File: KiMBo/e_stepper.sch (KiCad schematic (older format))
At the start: 24 parts, among them U19 TMC2130

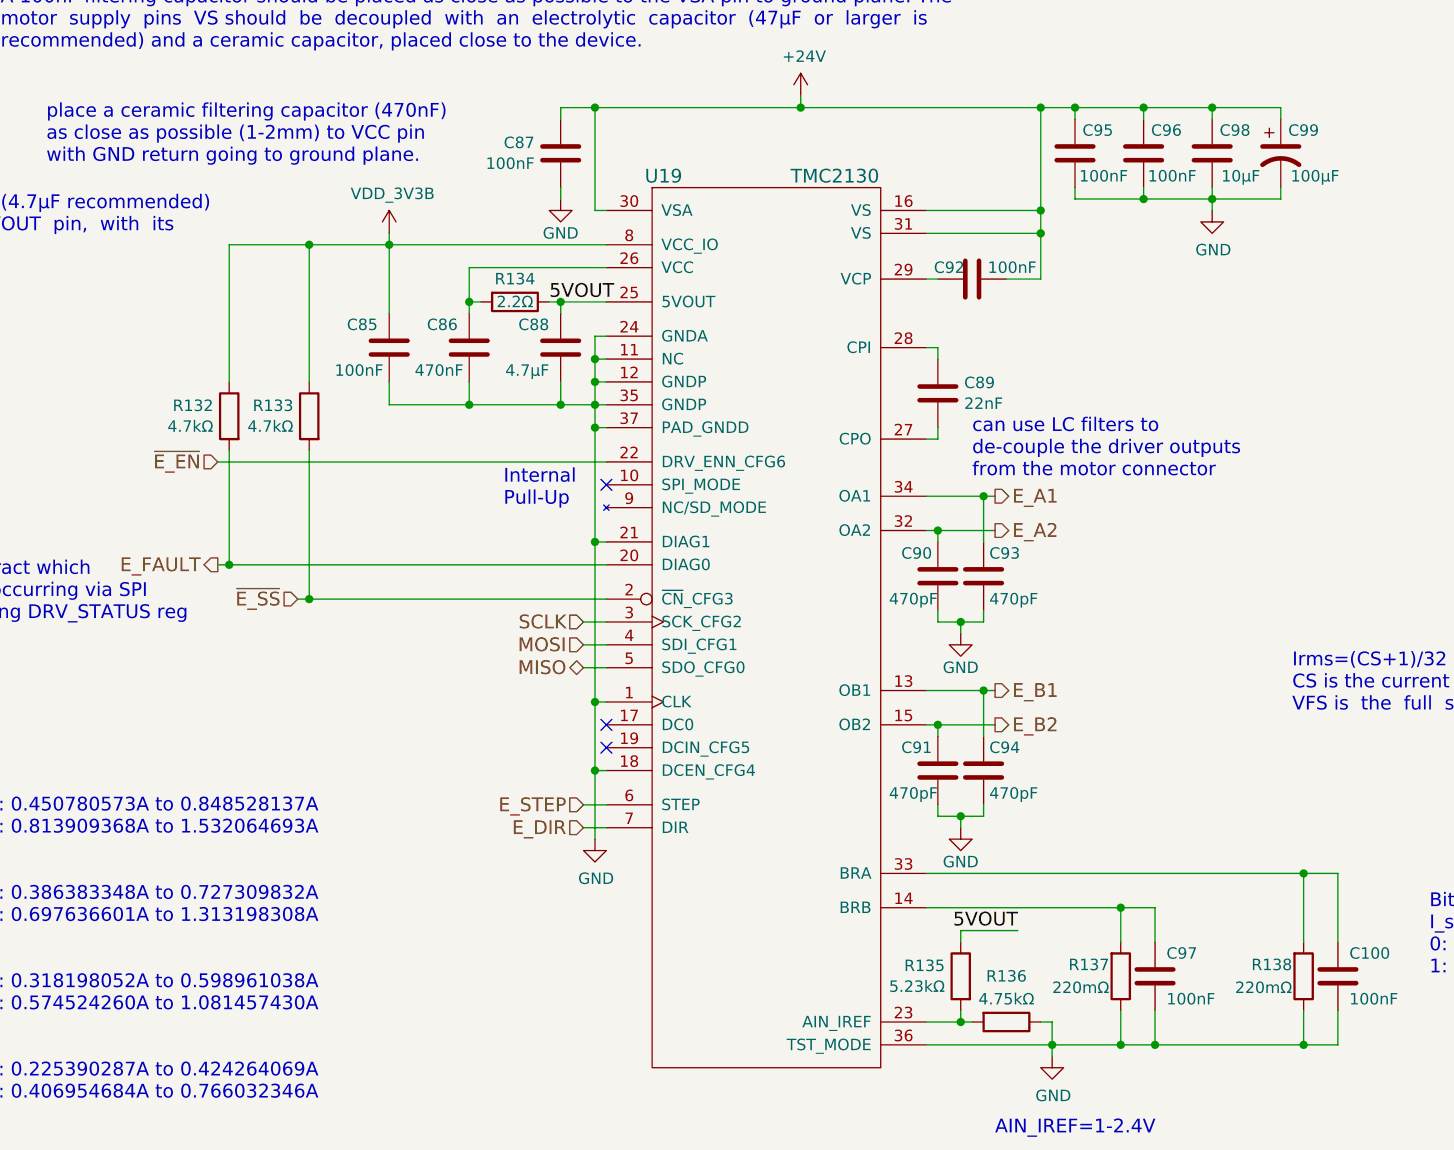
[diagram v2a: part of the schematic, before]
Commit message: Leave SPI0 free for a display, reassign pins so SPI1 is available
Fix some typos/errors
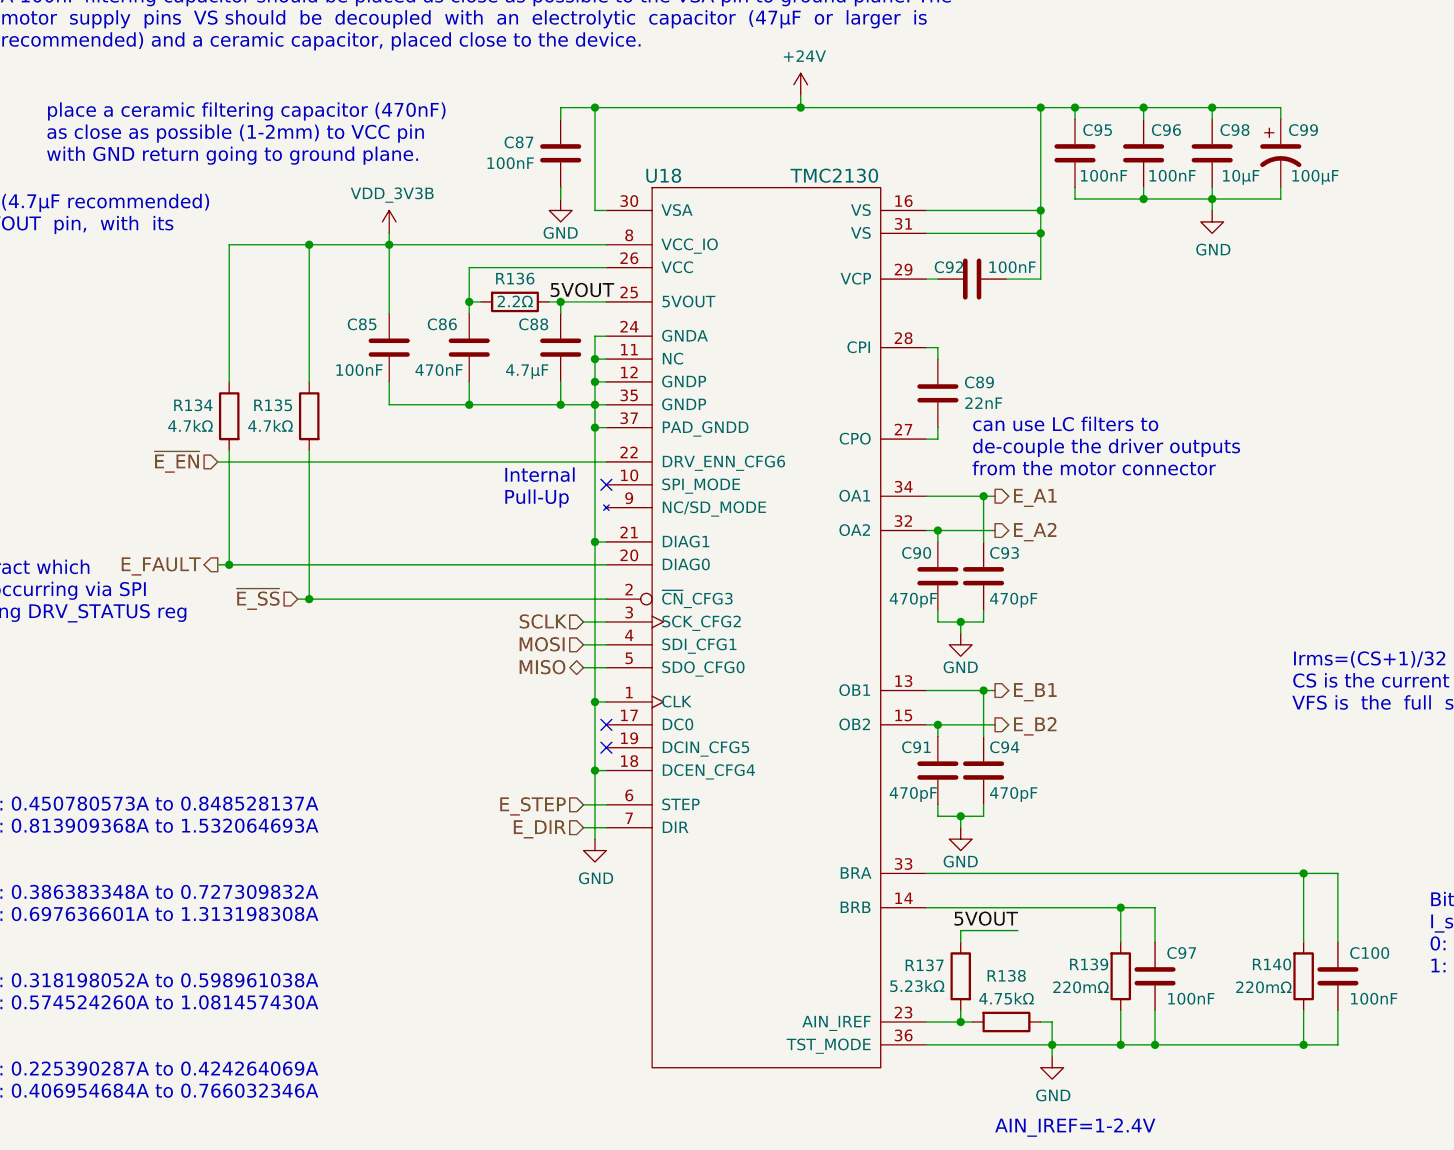
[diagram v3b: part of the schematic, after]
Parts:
- renumbered R132 to R134, R133 to R135, R134 to R136, R135 to R137, R136 to R138, R137 to R139, R138 to R140, U19 to U18
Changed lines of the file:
@@
 $EndComp
 $Comp
-L GND #PWR0200
+L GND #PWR0199
 U 1 1 589BD203
 P 7300 4150
-F 0 "#PWR0200" H 7300 3900 50  0001 C CNN
+F 0 "#PWR0199" H 7300 3900 50  0001 C CNN
 F 1 "GND" H 7300 4000 50  0000 C CNN
 F 2 "" H 7300 4150 50  0000 C CNN
@@
 $EndComp
 $Comp
-L GND #PWR0201
+L GND #PWR0200
 U 1 1 589BE47E
 P 10150 4200
-F 0 "#PWR0201" H 10150 3950 50  0001 C CNN
+F 0 "#PWR0200" H 10150 3950 50  0001 C CNN
 F 1 "GND" H 10155 4027 50  0000 C CNN
 F 2 "" H 10150 4200 50  0000 C CNN
@@
 $EndComp
 $Comp
-L +24V #PWR0202
+L +24V #PWR0201
 U 1 1 5BA7E125
 P 8350 3700
-F 0 "#PWR0202" H 8350 3550 50  0001 C CNN
+F 0 "#PWR0201" H 8350 3550 50  0001 C CNN
 F 1 "+24V" H 8365 3873 50  0000 C CNN
 F 2 "" H 8350 3700 50  0000 C CNN
@@
 $EndComp
 $Comp
-L R R138
+L R R140
 U 1 1 589C1BED
 P 10550 7550
-F 0 "R138" H 10500 7500 50  0000 R CNN
+F 0 "R140" H 10500 7500 50  0000 R CNN
 F 1 "220mΩ" H 10500 7600 50  0000 R CNN
 F 2 "" V 10480 7550 50  0001 C CNN
@@
 $EndComp
 $Comp
-L R R137
+L R R139
 U 1 1 589C1CA7
 P 9750 7550
-F 0 "R137" H 9700 7500 50  0000 R CNN
+F 0 "R139" H 9700 7500 50  0000 R CNN
 F 1 "220mΩ" H 9700 7600 50  0000 R CNN
 F 2 "" V 9680 7550 50  0001 C CNN
@@
 $EndComp
 $Comp
-L GND #PWR0203
+L GND #PWR0202
 U 1 1 5BA7E129
 P 9450 7900
-F 0 "#PWR0203" H 9450 7650 50  0001 C CNN
+F 0 "#PWR0202" H 9450 7650 50  0001 C CNN
 F 1 "GND" H 9455 7727 50  0000 C CNN
 F 2 "" H 9450 7900 50  0000 C CNN
@@
 NoConn ~ 7500 6450
 $Comp
-L R R134
+L R R136
 U 1 1 5BA7E12B
 P 7100 4600
-F 0 "R134" V 7000 4600 50  0000 C CNN
+F 0 "R136" V 7000 4600 50  0000 C CNN
 F 1 "2.2Ω" V 7100 4600 50  0000 C CNN
 F 2 "" V 7030 4600 50  0001 C CNN
@@
 NoConn ~ 7500 6550
 $Comp
-L GND #PWR0204
+L GND #PWR0203
 U 1 1 589C97FF
 P 7450 6950
-F 0 "#PWR0204" H 7450 6700 50  0001 C CNN
+F 0 "#PWR0203" H 7450 6700 50  0001 C CNN
 F 1 "GND" H 7455 6777 50  0000 C CNN
 F 2 "" H 7450 6950 50  0000 C CNN
@@
 E_FAULT
 $Comp
-L R R132
+L R R134
 U 1 1 589D21BC
 P 5850 5100
-F 0 "R132" H 5919 5146 50  0000 L CNN
+F 0 "R134" H 5919 5146 50  0000 L CNN
 F 1 "4.7kΩ" H 5919 5055 50  0000 L CNN
 F 2 "" V 5780 5100 50  0001 C CNN
@@
 5VOUT
 $Comp
-L R R135
+L R R137
 U 1 1 589E13FD
 P 9050 7550
-F 0 "R135" H 9119 7596 50  0000 L CNN
+F 0 "R137" H 9119 7596 50  0000 L CNN
 F 1 "5.23kΩ" H 9119 7505 50  0000 L CNN
 F 2 "" V 8980 7550 50  0001 C CNN
@@
 5VOUT
 $Comp
-L R R136
+L R R138
 U 1 1 589E24D4
 P 9250 7750
-F 0 "R136" V 9050 7750 50  0000 C CNN
+F 0 "R138" V 9050 7750 50  0000 C CNN
 F 1 "4.75kΩ" V 9150 7750 50  0000 C CNN
 F 2 "" V 9180 7750 50  0001 C CNN
@@
 AIN_IREF=1-2.4V
 $Comp
-L R R133
+L R R135
 U 1 1 5BA7E132
 P 6200 5100
-F 0 "R133" H 6269 5146 50  0000 L CNN
+F 0 "R135" H 6269 5146 50  0000 L CNN
 F 1 "4.7kΩ" H 6269 5055 50  0000 L CNN
 F 2 "" V 6130 5100 50  0001 C CNN
@@
 $EndComp
 $Comp
-L GND #PWR0205
+L GND #PWR0204
 U 1 1 58B19D33
 P 9050 6050
-F 0 "#PWR0205" H 9050 5800 50  0001 C CNN
+F 0 "#PWR0204" H 9050 5800 50  0001 C CNN
 F 1 "GND" H 9050 5900 50  0000 C CNN
 F 2 "" H 9050 6050 50  0000 C CNN
@@
 $EndComp
 $Comp
-L GND #PWR0206
+L GND #PWR0205
 U 1 1 58B1C704
 P 9050 6900
-F 0 "#PWR0206" H 9050 6650 50  0001 C CNN
+F 0 "#PWR0205" H 9050 6650 50  0001 C CNN
 F 1 "GND" H 9050 6750 50  0000 C CNN
 F 2 "" H 9050 6900 50  0000 C CNN
@@
 $EndComp
 $Comp
-L TMC2130 U19
+L TMC2130 U18
 U 1 1 5BA7E11D
 P 8200 5550
-F 0 "U19" H 7750 7050 60  0000 C CNN
+F 0 "U18" H 7750 7050 60  0000 C CNN
 F 1 "TMC2130" H 8500 7050 60  0000 C CNN
 F 2 "" H 8200 5850 60  0001 C CNN
@@
 Can extract which\nfault is occurring via SPI\nby reading DRV_STATUS reg
 $Comp
-L VDD_3V3B #PWR0207
+L VDD_3V3B #PWR0206
 U 1 1 5A2FD350
 P 6550 4300
-F 0 "#PWR0207" H 6550 4150 50  0001 C CNN
+F 0 "#PWR0206" H 6550 4150 50  0001 C CNN
 F 1 "VDD_3V3B" H 6565 4473 50  0000 C CNN
 F 2 "" H 6550 4300 50  0000 C CNN
